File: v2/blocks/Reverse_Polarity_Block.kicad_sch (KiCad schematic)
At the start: 5 parts, among them Q5 AP25P06K

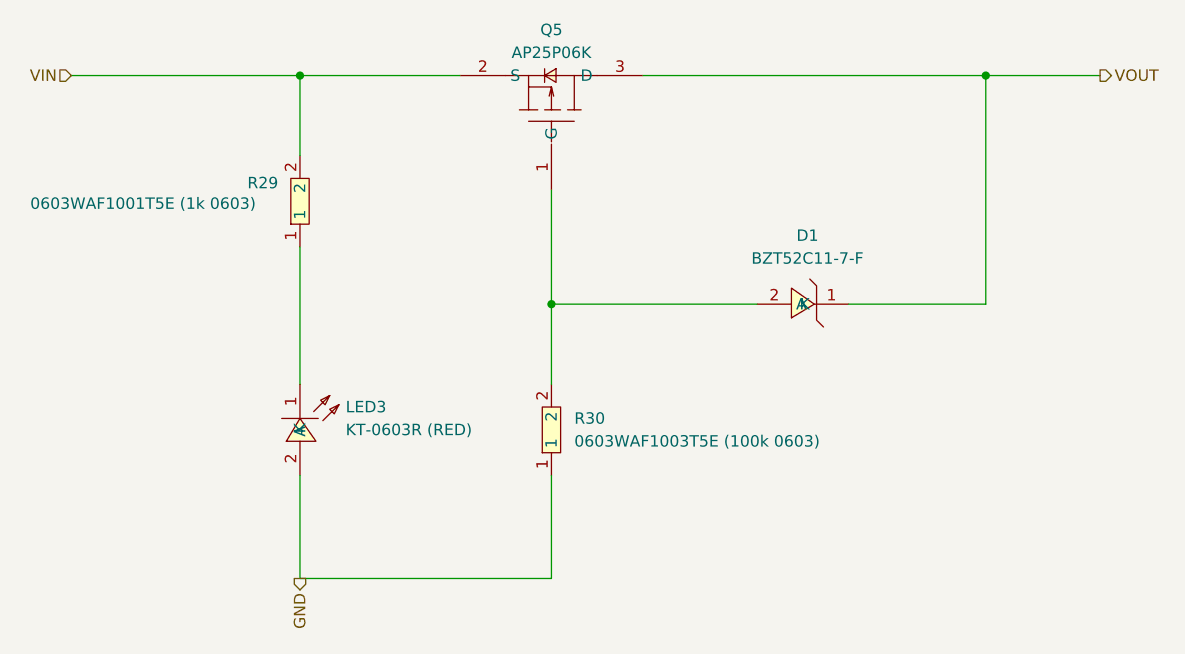
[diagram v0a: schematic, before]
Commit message: preliminary layout
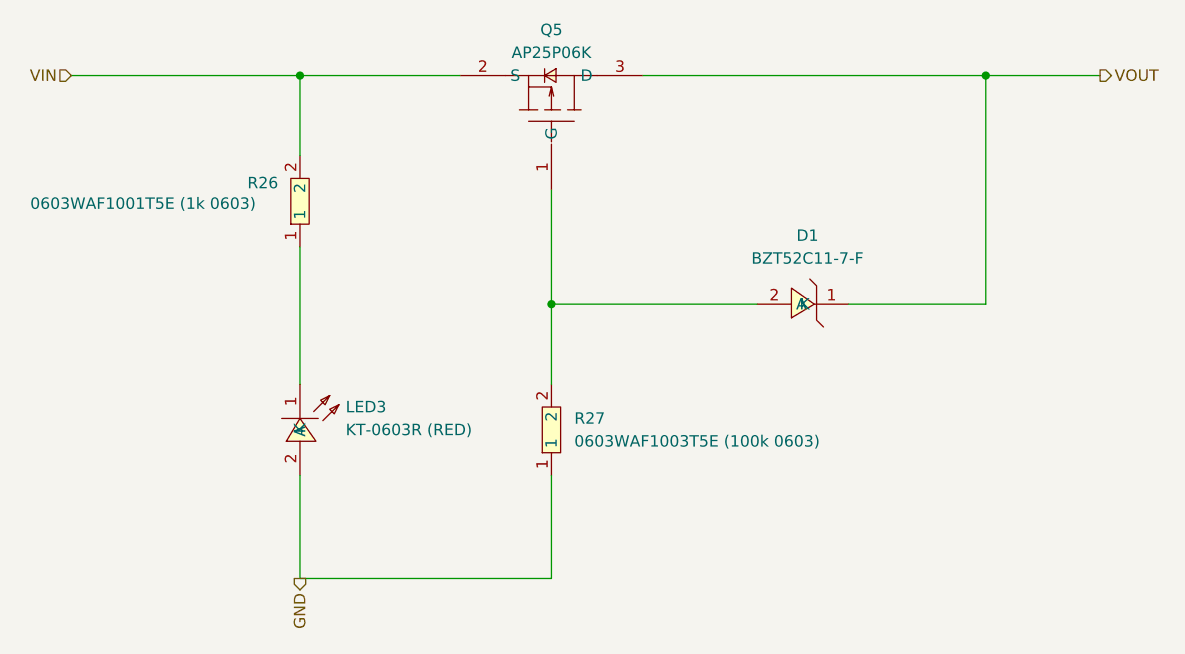
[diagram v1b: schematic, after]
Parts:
- renumbered R29 to R26, R30 to R27
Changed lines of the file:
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@@
 		(dnp no)
 		(fields_autoplaced yes)
-		(property "Reference" "R30"
+		(property "Reference" "R27"
 			(at 132.08 101.5999 90)
 			(effects
@@
 			(project "EPSv2"
 				(path "/61d36b12-c329-4dd2-b08b-b63678fc7b25/a84d95fe-b9be-4765-82ee-4700d1a0c14d"
-					(reference "R30")
+					(reference "R27")
 					(unit 1)
 				)
@@
 		(on_board yes)
 		(dnp no)
-		(property "Reference" "R29"
+		(property "Reference" "R26"
 			(at 95.758 75.438 90)
 			(effects
@@
 			(project "EPSv2"
 				(path "/61d36b12-c329-4dd2-b08b-b63678fc7b25/a84d95fe-b9be-4765-82ee-4700d1a0c14d"
-					(reference "R29")
+					(reference "R26")
 					(unit 1)
 				)

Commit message: routing done
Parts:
- renumbered D1 to D3, R26 to R27, R27 to R28
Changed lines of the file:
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@@
 		(dnp no)
 		(fields_autoplaced yes)
-		(property "Reference" "R27"
+		(property "Reference" "R28"
 			(at 132.08 101.5999 90)
 			(effects
@@
 			(project "EPSv2"
 				(path "/61d36b12-c329-4dd2-b08b-b63678fc7b25/a84d95fe-b9be-4765-82ee-4700d1a0c14d"
-					(reference "R27")
+					(reference "R28")
 					(unit 1)
 				)
@@
 		(dnp no)
 		(fields_autoplaced yes)
-		(property "Reference" "D1"
+		(property "Reference" "D3"
 			(at 157.99 81.28 0)
 			(effects
@@
 			(project "EPSv2"
 				(path "/61d36b12-c329-4dd2-b08b-b63678fc7b25/a84d95fe-b9be-4765-82ee-4700d1a0c14d"
-					(reference "D1")
+					(reference "D3")
 					(unit 1)
 				)
@@
 		(on_board yes)
 		(dnp no)
-		(property "Reference" "R26"
+		(property "Reference" "R27"
 			(at 95.758 75.438 90)
 			(effects
@@
 			(project "EPSv2"
 				(path "/61d36b12-c329-4dd2-b08b-b63678fc7b25/a84d95fe-b9be-4765-82ee-4700d1a0c14d"
-					(reference "R26")
+					(reference "R27")
 					(unit 1)
 				)

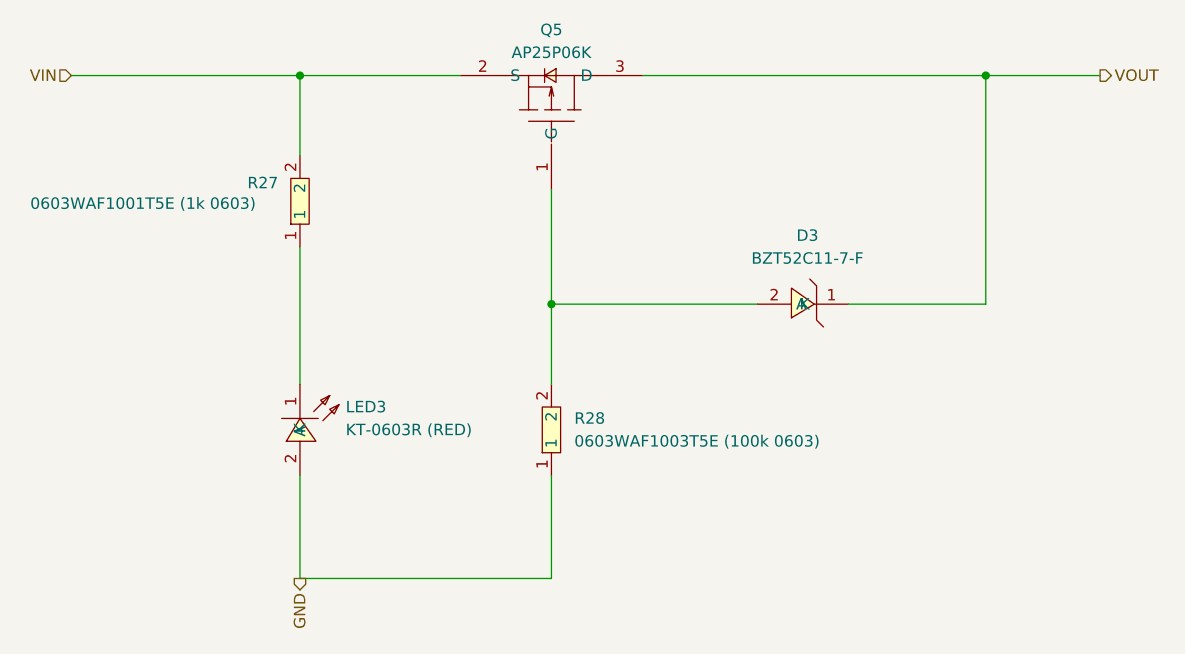
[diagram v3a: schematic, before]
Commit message: can transceiver and battery reverse polarity bypass
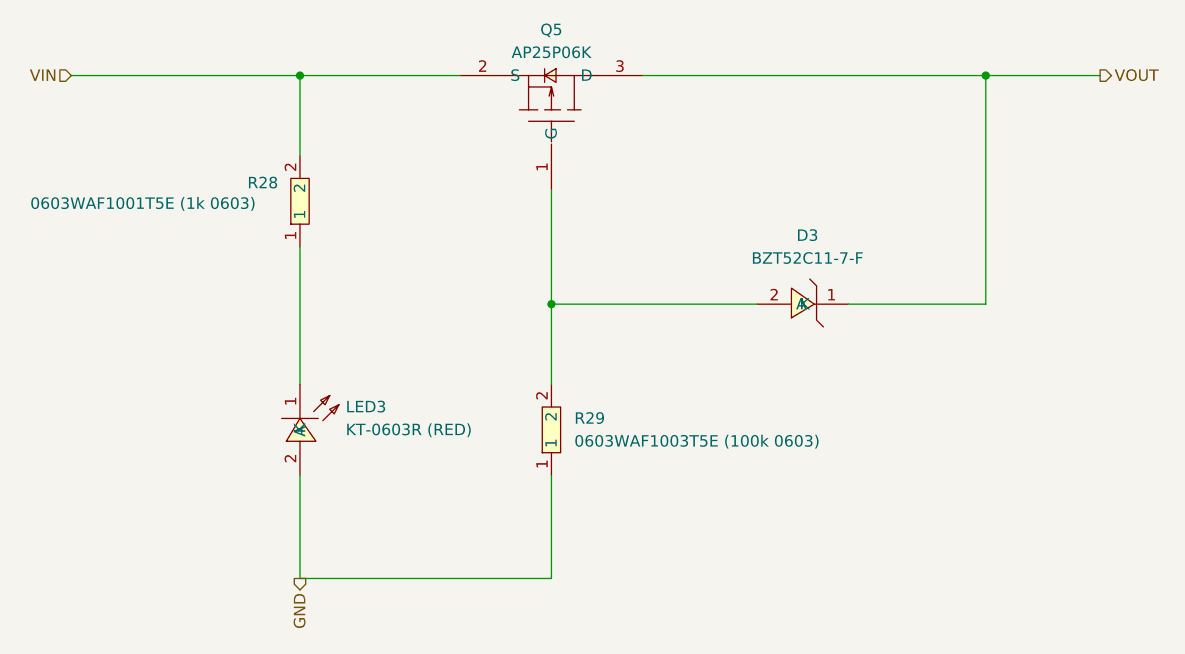
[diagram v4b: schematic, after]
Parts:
- renumbered R27 to R28, R28 to R29
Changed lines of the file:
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@@
 		(shape output)
 		(at 101.6 119.38 270)
+		(fields_autoplaced yes)
 		(effects
 			(font
@@
 		(shape input)
 		(at 76.2 63.5 180)
+		(fields_autoplaced yes)
 		(effects
 			(font
@@
 		(shape output)
 		(at 190.5 63.5 0)
+		(fields_autoplaced yes)
 		(effects
 			(font
@@
 		(dnp no)
 		(fields_autoplaced yes)
-		(property "Reference" "R28"
+		(property "Reference" "R29"
 			(at 132.08 101.5999 90)
 			(effects
@@
 			(project "EPSv2"
 				(path "/61d36b12-c329-4dd2-b08b-b63678fc7b25/a84d95fe-b9be-4765-82ee-4700d1a0c14d"
-					(reference "R28")
+					(reference "R29")
 					(unit 1)
 				)
@@
 		(on_board yes)
 		(dnp no)
-		(property "Reference" "R27"
+		(property "Reference" "R28"
 			(at 95.758 75.438 90)
 			(effects
@@
 			(project "EPSv2"
 				(path "/61d36b12-c329-4dd2-b08b-b63678fc7b25/a84d95fe-b9be-4765-82ee-4700d1a0c14d"
-					(reference "R27")
+					(reference "R28")
 					(unit 1)
 				)
